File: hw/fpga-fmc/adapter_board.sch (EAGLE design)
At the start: 175 parts, among them IC1 M24C02, J1 5569262-1, J2 ASP-134488-01, U1 ADM3066E, U10 ADM3066E, U11 ADM3066E, U12 ADM3066E, U13 ADM3066E, U14 ADM3066E, U15 ADM3066E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

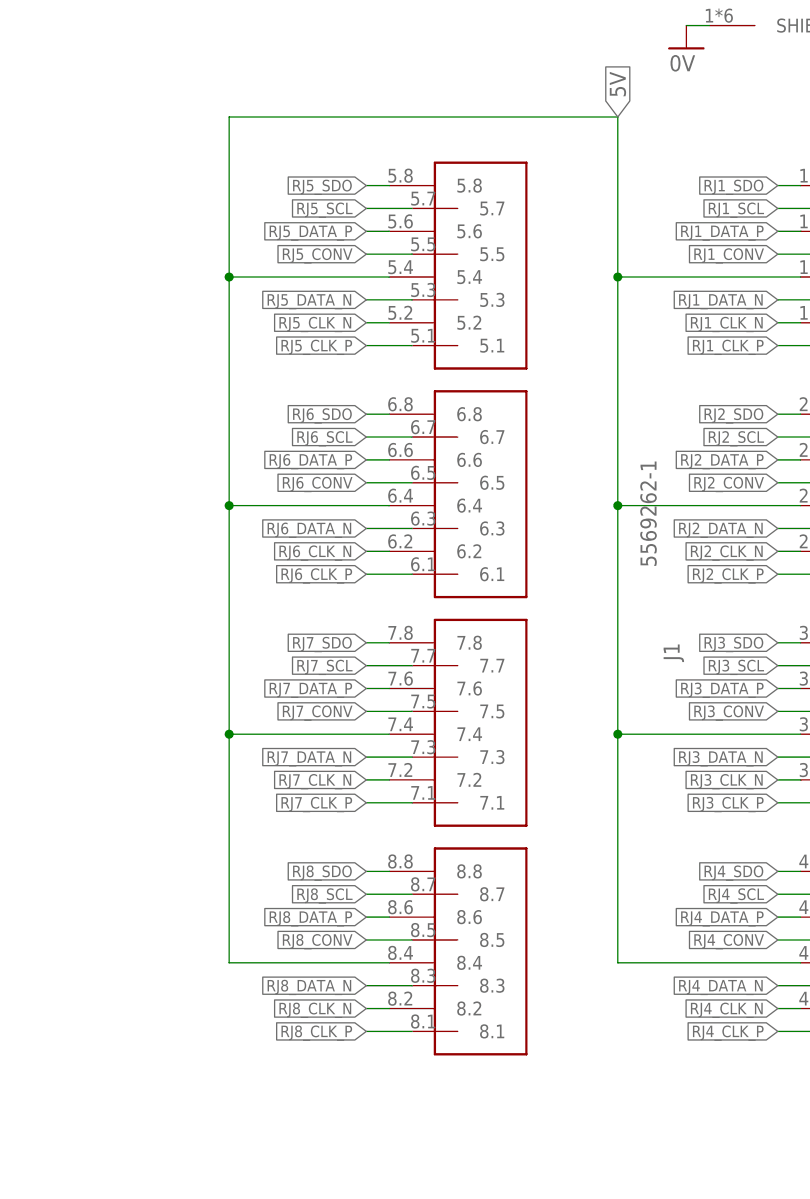
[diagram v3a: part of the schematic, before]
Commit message: hw/fpga-fmc: fix wrong connection on bottom row rj-45 connectors
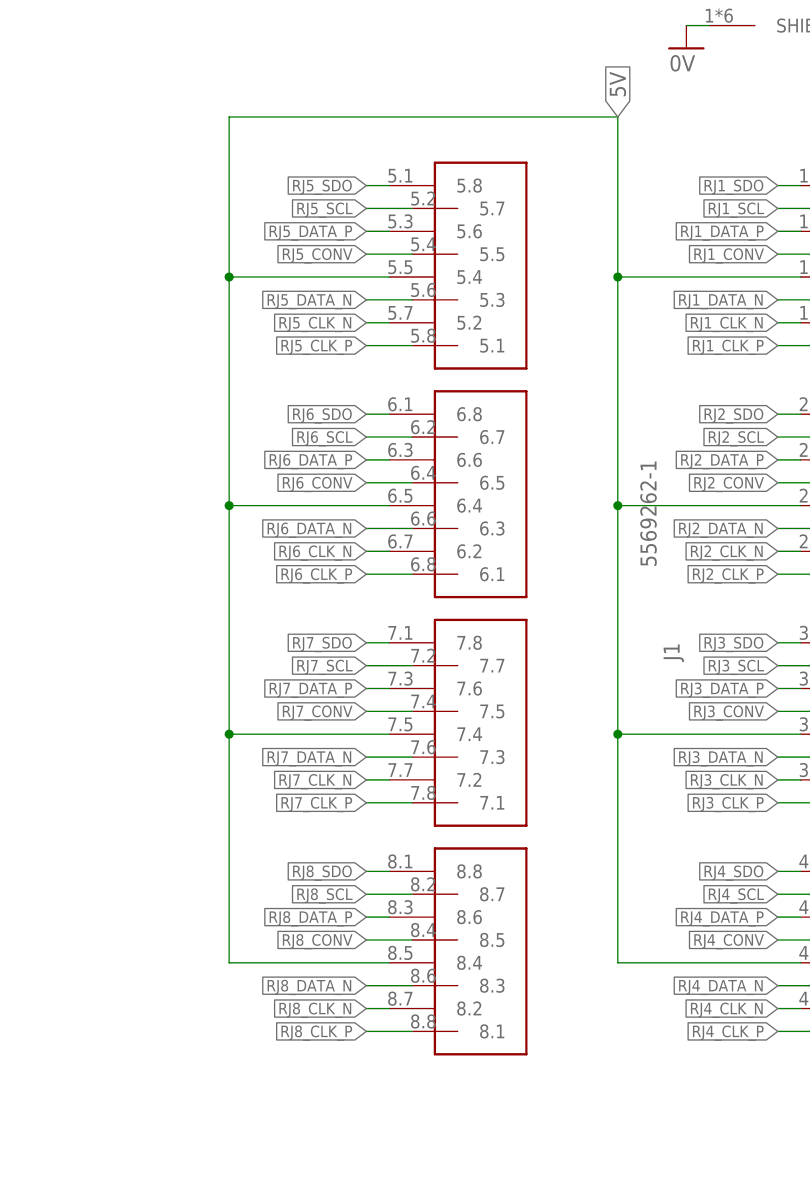
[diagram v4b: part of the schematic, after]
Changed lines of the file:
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@@
 <grid distance="0.1" unitdist="inch" unit="inch" style="lines" multiple="1" display="no" altdistance="0.01" altunitdist="inch" altunit="inch"/>
 <layers>
-<layer number="1" name="Top" color="4" fill="1" visible="yes" active="no"/>
-<layer number="2" name="Route2" color="16" fill="1" visible="yes" active="no"/>
-<layer number="3" name="Route3" color="17" fill="1" visible="yes" active="no"/>
-<layer number="4" name="Route4" color="18" fill="1" visible="yes" active="no"/>
-<layer number="5" name="Route5" color="19" fill="1" visible="yes" active="no"/>
-<layer number="6" name="Route6" color="25" fill="1" visible="yes" active="no"/>
-<layer number="7" name="Route7" color="26" fill="1" visible="yes" active="no"/>
-<layer number="8" name="Route8" color="27" fill="1" visible="yes" active="no"/>
-<layer number="9" name="Route9" color="28" fill="1" visible="yes" active="no"/>
-<layer number="10" name="Route10" color="29" fill="1" visible="yes" active="no"/>
-<layer number="11" name="Route11" color="30" fill="1" visible="yes" active="no"/>
-<layer number="12" name="Route12" color="20" fill="1" visible="yes" active="no"/>
-<layer number="13" name="Route13" color="21" fill="1" visible="yes" active="no"/>
-<layer number="14" name="Route14" color="22" fill="1" visible="yes" active="no"/>
-<layer number="15" name="Route15" color="23" fill="1" visible="yes" active="no"/>
-<layer number="16" name="Bottom" color="1" fill="1" visible="yes" active="no"/>
-<layer number="17" name="Pads" color="2" fill="1" visible="yes" active="no"/>
-<layer number="18" name="Vias" color="2" fill="1" visible="yes" active="no"/>
-<layer number="19" name="Unrouted" color="6" fill="1" visible="yes" active="no"/>
-<layer number="20" name="Dimension" color="24" fill="1" visible="yes" active="no"/>
-<layer number="21" name="tPlace" color="7" fill="1" visible="yes" active="no"/>
-<layer number="22" name="bPlace" color="7" fill="1" visible="yes" active="no"/>
-<layer number="23" name="tOrigins" color="15" fill="1" visible="yes" active="no"/>
-<layer number="24" name="bOrigins" color="15" fill="1" visible="yes" active="no"/>
-<layer number="25" name="tNames" color="7" fill="1" visible="yes" active="no"/>
-<layer number="26" name="bNames" color="7" fill="1" visible="yes" active="no"/>
-<layer number="27" name="tValues" color="7" fill="1" visible="yes" active="no"/>
-<layer number="28" name="bValues" color="7" fill="1" visible="yes" active="no"/>
+<layer number="1" name="Top" color="4" fill="1" visible="no" active="no"/>
+<layer number="2" name="Route2" color="16" fill="1" visible="no" active="no"/>
+<layer number="3" name="Route3" color="17" fill="1" visible="no" active="no"/>
+<layer number="4" name="Route4" color="18" fill="1" visible="no" active="no"/>
+<layer number="5" name="Route5" color="19" fill="1" visible="no" active="no"/>
+<layer number="6" name="Route6" color="25" fill="1" visible="no" active="no"/>
+<layer number="7" name="Route7" color="26" fill="1" visible="no" active="no"/>
+<layer number="8" name="Route8" color="27" fill="1" visible="no" active="no"/>
+<layer number="9" name="Route9" color="28" fill="1" visible="no" active="no"/>
+<layer number="10" name="Route10" color="29" fill="1" visible="no" active="no"/>
+<layer number="11" name="Route11" color="30" fill="1" visible="no" active="no"/>
+<layer number="12" name="Route12" color="20" fill="1" visible="no" active="no"/>
+<layer number="13" name="Route13" color="21" fill="1" visible="no" active="no"/>
+<layer number="14" name="Route14" color="22" fill="1" visible="no" active="no"/>
+<layer number="15" name="Route15" color="23" fill="1" visible="no" active="no"/>
+<layer number="16" name="Bottom" color="1" fill="1" visible="no" active="no"/>
+<layer number="17" name="Pads" color="2" fill="1" visible="no" active="no"/>
+<layer number="18" name="Vias" color="2" fill="1" visible="no" active="no"/>
+<layer number="19" name="Unrouted" color="6" fill="1" visible="no" active="no"/>
+<layer number="20" name="Dimension" color="24" fill="1" visible="no" active="no"/>
+<layer number="21" name="tPlace" color="7" fill="1" visible="no" active="no"/>
+<layer number="22" name="bPlace" color="7" fill="1" visible="no" active="no"/>
+<layer number="23" name="tOrigins" color="15" fill="1" visible="no" active="no"/>
+<layer number="24" name="bOrigins" color="15" fill="1" visible="no" active="no"/>
+<layer number="25" name="tNames" color="7" fill="1" visible="no" active="no"/>
+<layer number="26" name="bNames" color="7" fill="1" visible="no" active="no"/>
+<layer number="27" name="tValues" color="7" fill="1" visible="no" active="no"/>
+<layer number="28" name="bValues" color="7" fill="1" visible="no" active="no"/>
 <layer number="29" name="tStop" color="7" fill="3" visible="no" active="no"/>
 <layer number="30" name="bStop" color="7" fill="6" visible="no" active="no"/>
@@
 <layer number="35" name="tGlue" color="7" fill="4" visible="no" active="no"/>
 <layer number="36" name="bGlue" color="7" fill="5" visible="no" active="no"/>
-<layer number="37" name="tTest" color="7" fill="1" visible="yes" active="no"/>
-<layer number="38" name="bTest" color="7" fill="1" visible="yes" active="no"/>
+<layer number="37" name="tTest" color="7" fill="1" visible="no" active="no"/>
+<layer number="38" name="bTest" color="7" fill="1" visible="no" active="no"/>
 <layer number="39" name="tKeepout" color="4" fill="11" visible="no" active="no"/>
 <layer number="40" name="bKeepout" color="1" fill="11" visible="no" active="no"/>
@@
 <layer number="44" name="Drills" color="7" fill="1" visible="no" active="no"/>
 <layer number="45" name="Holes" color="7" fill="1" visible="no" active="no"/>
-<layer number="46" name="Milling" color="3" fill="1" visible="yes" active="no"/>
-<layer number="47" name="Measures" color="7" fill="1" visible="yes" active="no"/>
-<layer number="48" name="Document" color="7" fill="1" visible="yes" active="no"/>
-<layer number="49" name="Reference" color="7" fill="1" visible="yes" active="no"/>
-<layer number="50" name="dxf" color="7" fill="1" visible="yes" active="no"/>
-<layer number="51" name="tDocu" color="7" fill="1" visible="yes" active="no"/>
-<layer number="52" name="bDocu" color="7" fill="1" visible="yes" active="no"/>
-<layer number="53" name="tGND_GNDA" color="7" fill="9" visible="yes" active="no"/>
-<layer number="54" name="bGND_GNDA" color="1" fill="9" visible="yes" active="no"/>
-<layer number="56" name="wert" color="7" fill="1" visible="yes" active="no"/>
+<layer number="46" name="Milling" color="3" fill="1" visible="no" active="no"/>
+<layer number="47" name="Measures" color="7" fill="1" visible="no" active="no"/>
+<layer number="48" name="Document" color="7" fill="1" visible="no" active="no"/>
+<layer number="49" name="Reference" color="7" fill="1" visible="no" active="no"/>
+<layer number="50" name="dxf" color="7" fill="1" visible="no" active="no"/>
+<layer number="51" name="tDocu" color="7" fill="1" visible="no" active="no"/>
+<layer number="52" name="bDocu" color="7" fill="1" visible="no" active="no"/>
+<layer number="53" name="tGND_GNDA" color="7" fill="9" visible="no" active="no"/>
+<layer number="54" name="bGND_GNDA" color="1" fill="9" visible="no" active="no"/>
+<layer number="56" name="wert" color="7" fill="1" visible="no" active="no"/>
 <layer number="88" name="SimResults" color="9" fill="1" visible="yes" active="yes"/>
 <layer number="89" name="SimProbes" color="9" fill="1" visible="yes" active="yes"/>
